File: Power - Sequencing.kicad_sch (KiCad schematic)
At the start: 0 parts

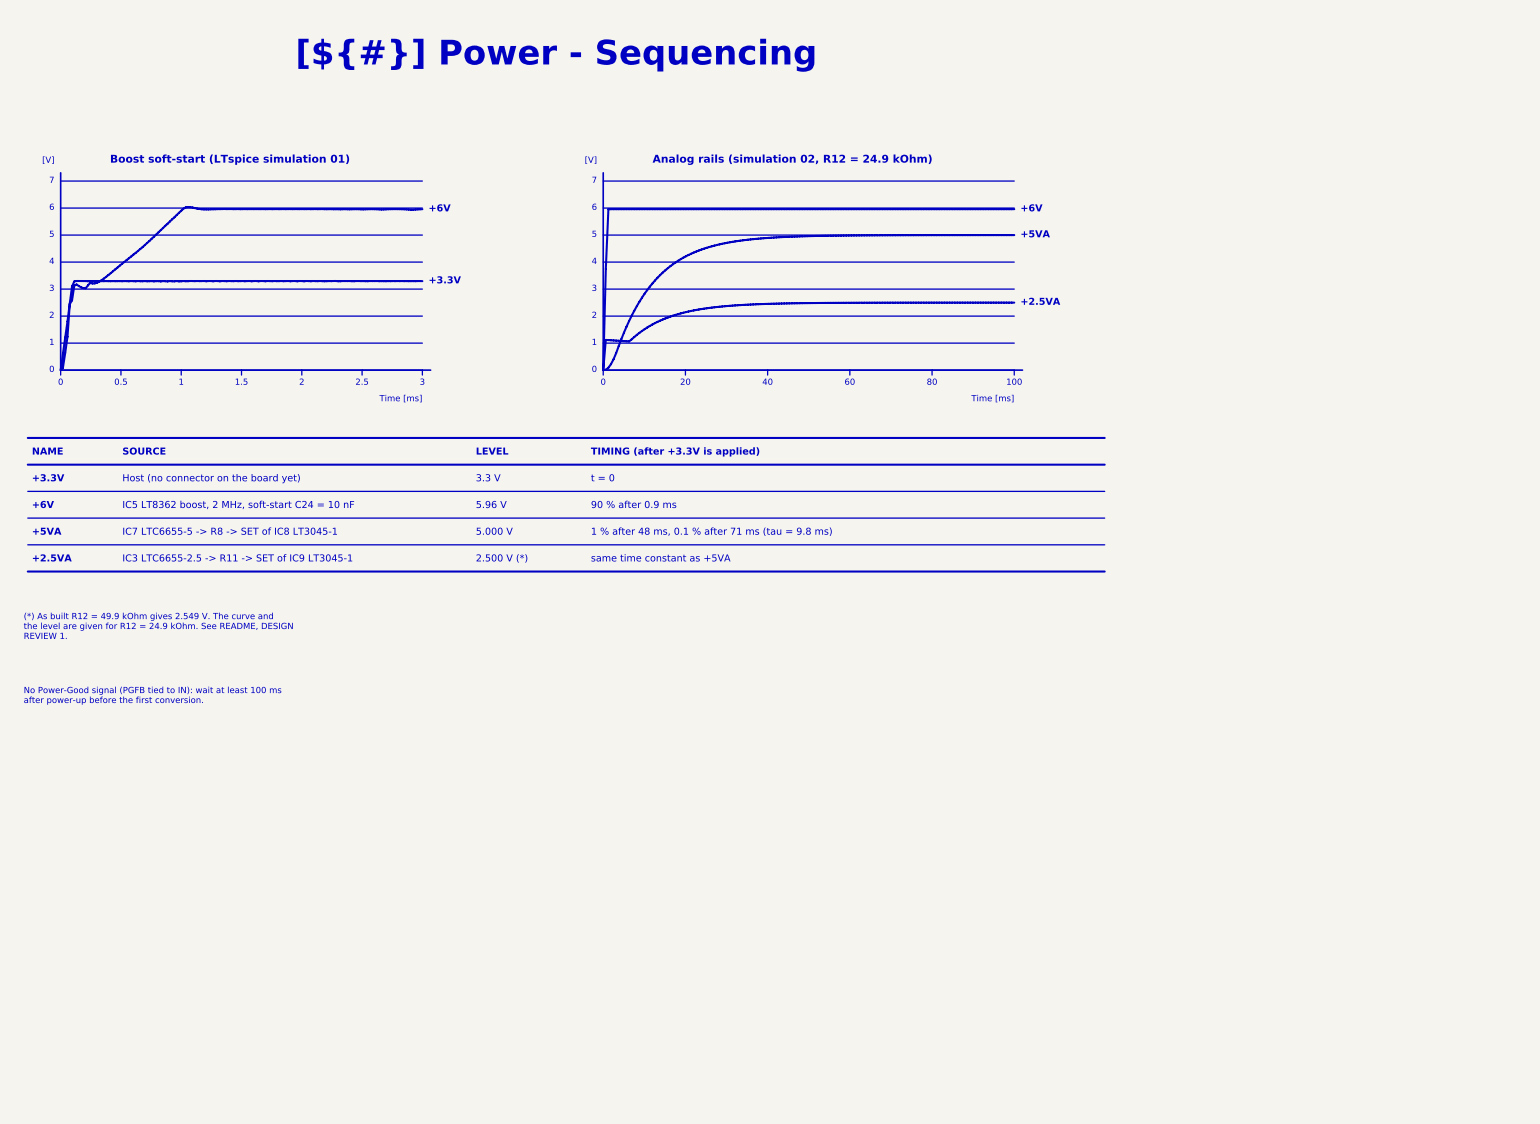
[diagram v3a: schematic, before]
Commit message: Restyle schematic sheets, new title block logo, WE-MAPI inductor in simulations
- Schematic sheets: restyled frames, tables and text boxes
- Title block: INGENIERIE FRANCE logo in KDT_Template_GIT.kicad_wks
- LTspice: L1 modelled as WE-MAPI 4030 74438357022 (22 mOhm),
  simulations 01 and 03 rerun, README and results updated

Co-Authored-By: Claude Opus 5.5 <noreply@anthropic.com>
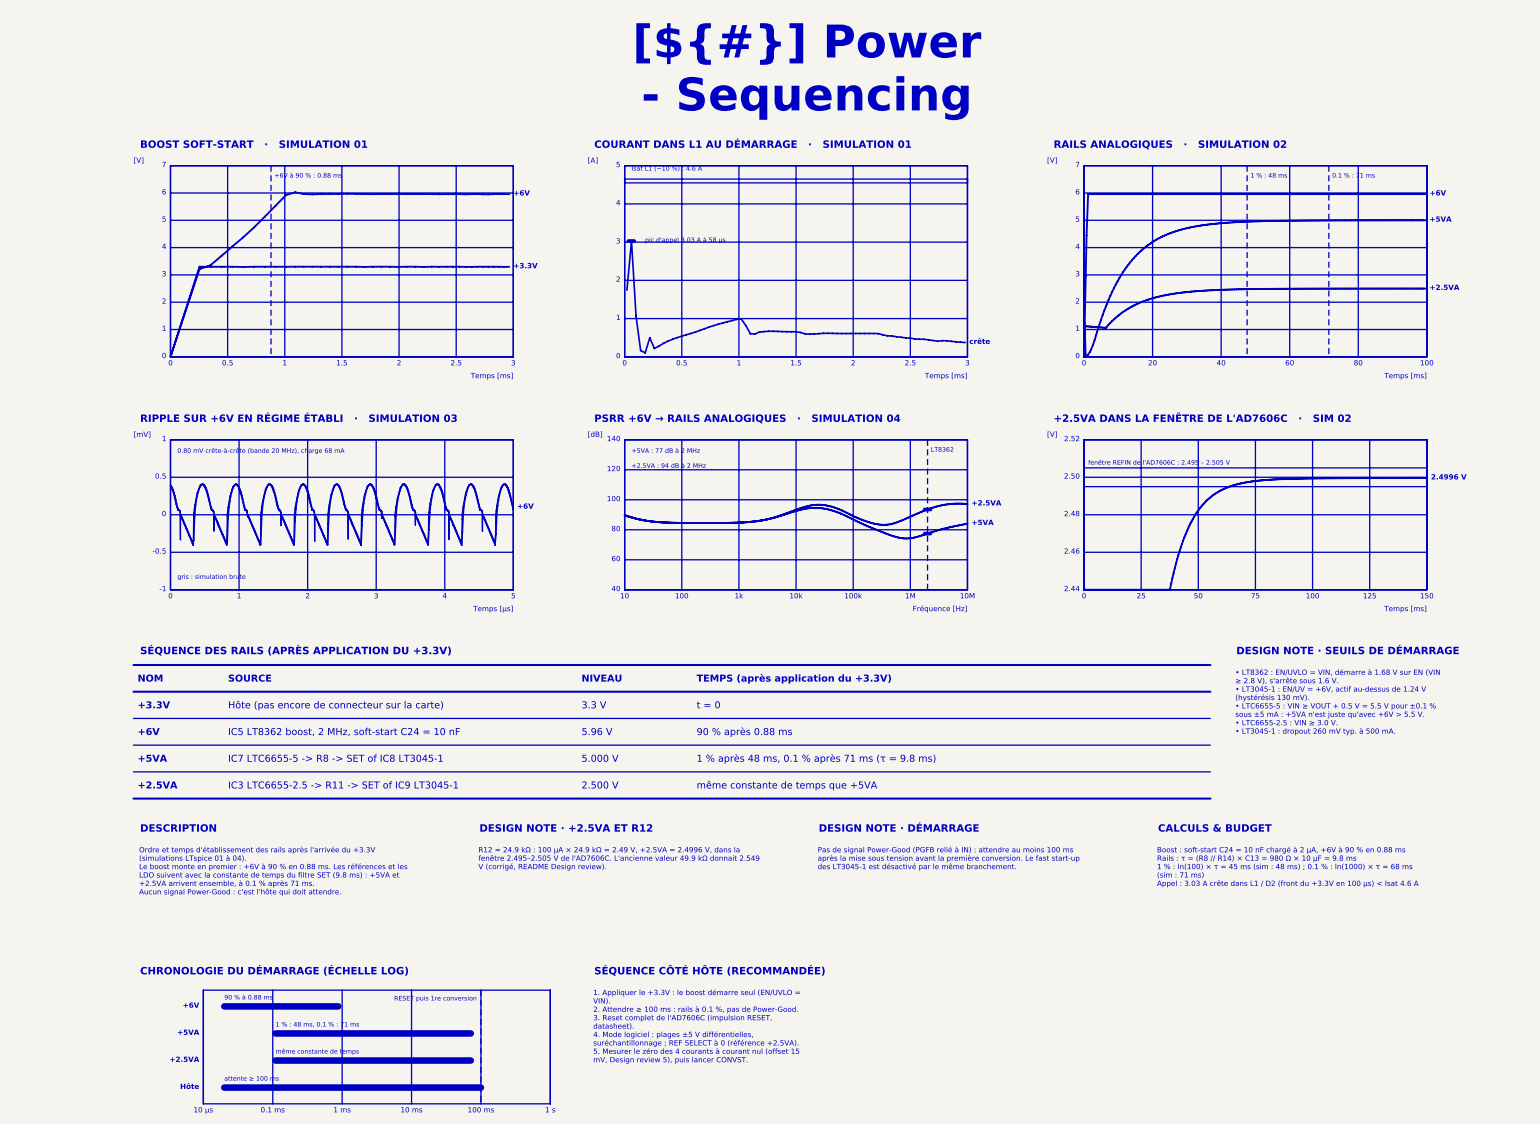
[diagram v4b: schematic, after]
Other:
- note added: "+2.5VA : 94 dB à 2 MHz"
- note added: "+5VA : 77 dB à 2 MHz"
- note added: "+6V à 90 % : 0.88 ms"
- note added: "-0.5"
- note added: "-1"
- note added: "0.1 % : 71 ms"
- note added: "0.1 ms"
- note added: "0.80 mV crête-à-crête (bande 20 MHz), charge 68 mA"
- note added: "1 % : 48 ms"
- note added: "1 % : 48 ms, 0.1 % : 71 ms"
- note added: "1 % après 48 ms, 0.1 % après 71 ms (τ = 9.8 ms)"
- note added: "1 ms"
- note added: "1 s"
- note added: "10"
- note added: "10 ms"
- note added: "10 µs"
- note added: "100 ms"
- note added: "100k"
- note added: "10M"
- note added: "10k"
- note added: "120"
- note added: "125"
- note added: "140"
- note added: "150"
- note added: "1M"
- note added: "1k"
- note added: "2.44"
- note added: "2.46"
- note added: "2.48"
- note added: "2.4996 V"
- note added: "2.50"
- note added: "2.500 V"
- note added: "2.52"
- note added: "25"
- note added: "50"
- note added: "75"
- note added: "90 % après 0.88 ms"
- note added: "90 % à 0.88 ms"
- note added: "Fréquence [Hz]"
- note added: "Hôte"
- note added: "Hôte (pas encore de connecteur sur la carte)"
- note added: "Isat L1 (−10 %) : 4.6 A"
- note added: "LT8362"
- note added: "NIVEAU"
- note added: "NOM"
- note added: "RESET puis 1re conversion"
- note added: "TEMPS (après application du +3.3V)"
- note added: "Temps [ms]"
- note added: "Temps [µs]"
- note added: "[A]"
- note added: "[dB]"
- note added: "[mV]"
- note added: "attente ≥ 100 ms"
- note added: "crête"
- note added: "fenêtre REFIN de l'AD7606C : 2.495 – 2.505 V"
- note added: "gris : simulation brute"
- note added: "même constante de temps"
- note added: "même constante de temps que +5VA"
- note added: "pic d'appel 3.03 A à 58 µs"
- note removed: "1 % after 48 ms, 0.1 % after 71 ms (tau = 9.8 ms)"
- note removed: "2.500 V (*)"
- note removed: "90 % after 0.9 ms"
- note removed: "Analog rails (simulation 02, R12 = 24.9 kOhm)"
- note removed: "Boost soft-start (LTspice simulation 01)"
- note removed: "Host (no connector on the board yet)"
- note removed: "LEVEL"
- note removed: "NAME"
- note removed: "TIMING (after +3.3V is applied)"
- note removed: "Time [ms]"
- note removed: "same time constant as +5VA"

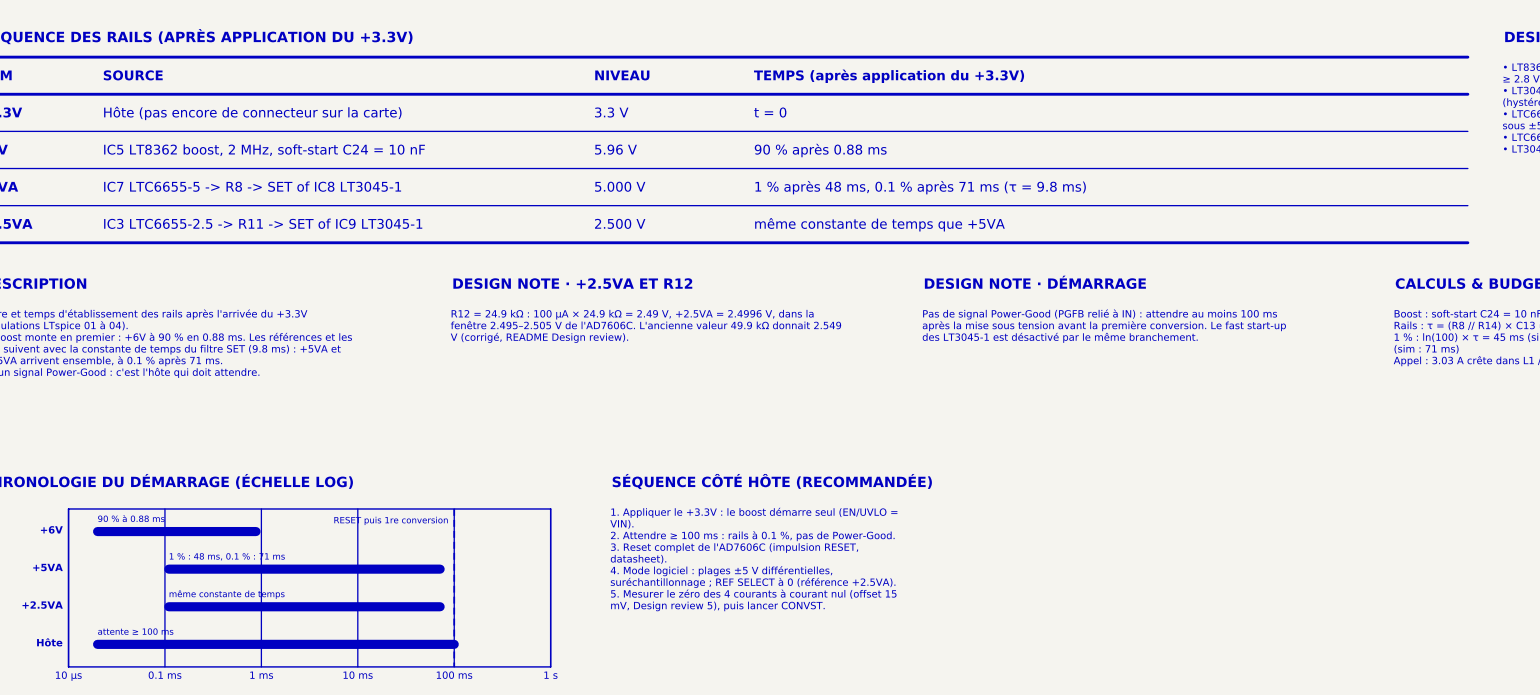
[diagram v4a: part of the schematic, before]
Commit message: Wire the AD7606C-18 digital side to host header J4, add test points
- AD7606C-18: software mode (OS0-2 high), serial (PAR/SER SEL high),
  REF SELECT low; CONVST, BUSY, RESET, CS, SCLK, SDI, FRSTDATA and
  DOUTA-D to J4 (2x8 pin header 2.54 mm, horizontal), +3.3V on J4 pin 1
- AD7606C-18 AGND pin 26 and REFGND pin 46 on GND
- Test points TP1-TP16: rails, INA241 outputs, CONVST, BUSY
- Nets renamed SHUNT_*, INA_*, ADC_*; net colours in the project
- LT3045-1 footprint: thermal vias numbered as exposed pad 13
- PCB updated from the schematic; ADC_* digital nets not routed yet
- README template / CHANGELOG: status, J4 pinout, design review 1 and 2
  fixed, new finding 9 (VDRIVE above AVCC + 0.3 V at power-up),
  4 channels / 8 ADC inputs

Co-Authored-By: Claude Opus 5.5 <noreply@anthropic.com>
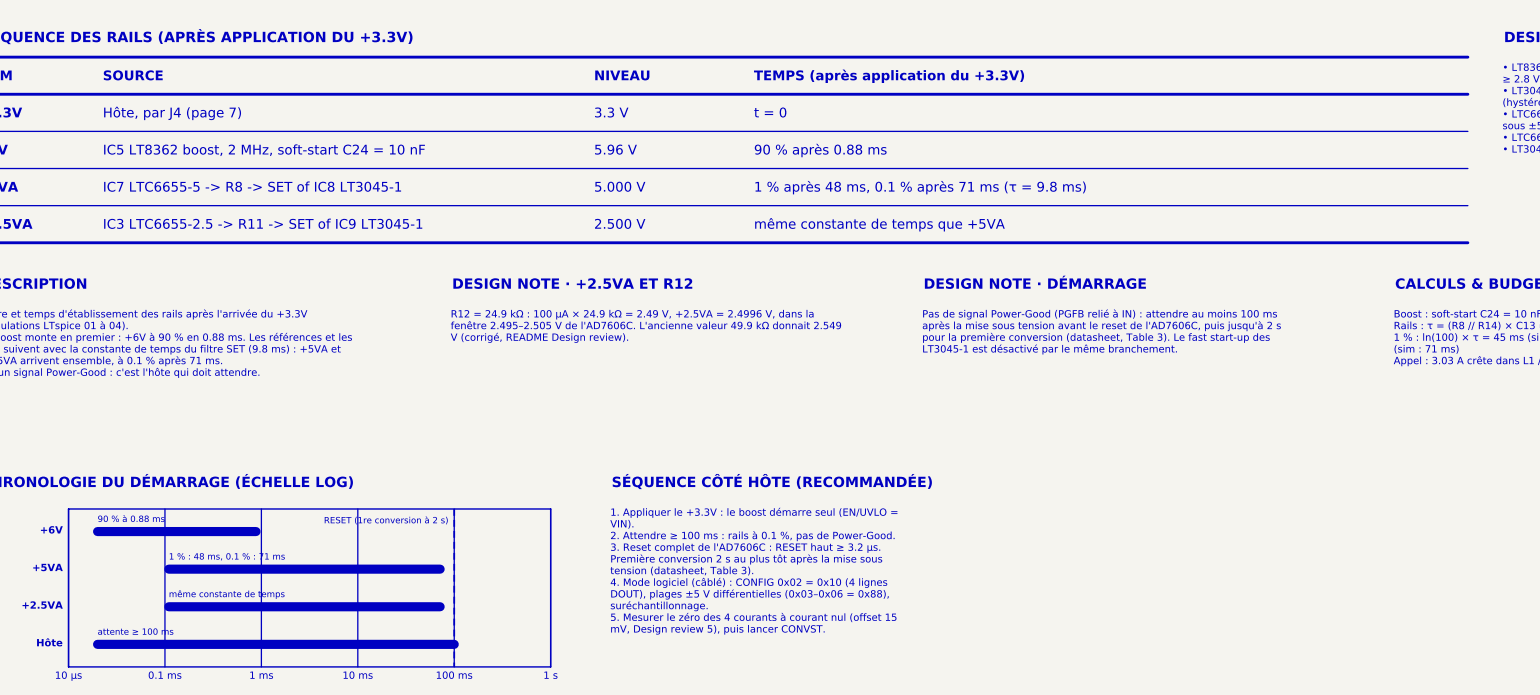
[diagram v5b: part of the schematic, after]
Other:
- note added: "Hôte, par J4 (page 7)"
- note added: "RESET (1re conversion à 2 s)"
- note removed: "Hôte (pas encore de connecteur sur la carte)"
- note removed: "RESET puis 1re conversion"
